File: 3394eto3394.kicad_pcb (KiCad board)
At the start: 2 copper layers, 21.5 x 31.2 mm, 11 parts, among them J1 Conn_01x20_Male, J2 Conn_01x02_Male, J3 Conn_01x02_Male, J4 Conn_01x02_Male, U1 AS3394E

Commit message: Version 2
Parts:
- removed J3, J4: Conn_01x02_Male, Connector_PinHeader_2.54mm:PinHeader_1x02_P2.54mm_Vertical
- added C1: 100n, Capacitor_THT:C_Rect_L7.0mm_W3.5mm_P2.50mm_P5.00mm, F.Cu at (57.1, 29.5)
- added C2: 100n, Capacitor_THT:C_Rect_L7.0mm_W3.5mm_P2.50mm_P5.00mm, F.Cu at (38.4, 34.4)
- J2: value Conn_01x02_Male -> Conn_01x04_Male; footprint Connector_PinHeader_2.54mm:PinHeader_1x02_P2.54mm_Vertical -> Connector_PinHeader_2.54mm:PinHeader_1x04_P2.54mm_Vertical
- R3: value 1k -> 500R
- moved J2 13.7 mm to (38.1, 43.8)
- moved D1 9.24 mm to (57.2, 42.2)
- moved D2 9.24 mm to (57.2, 37.2)
- moved D3 9.24 mm to (57.2, 47.2)
- moved D4 9.24 mm to (57.2, 52.2)
- moved R1 9.12 mm to (38.9, 37.5), turned to 180 degrees
- moved R3 7.90 mm to (52.7, 57.8), turned to 0 degrees
- moved J1 6.35 mm to (45.9, 29.8)
- moved U1 6.35 mm to (42.0, 29.8)
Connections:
- J1 pad 9: /EXT_IN -> /NOISE_IN
- J2 pad 2: GND -> /SAW_OUT
- U1 pad 11: /EXT_IN1 -> /NOISE_IN
- U1 pad 14: /EXT_IN -> /EXT_IN1
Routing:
- net /EXT_IN1: track 10.8 -> 33.9 mm, vias 0 -> 2
- net /NOISE_IN: track 0.00 -> 7.96 mm
- net /EXT_IN: track 6.61 -> 0.00 mm
- net /Cs: track 9.33 -> 15.3 mm
- net -VSW: track 3.92 -> 9.50 mm
- net +VSW: track 3.92 -> 9.18 mm
- net /SUB_OUT: track 9.53 -> 5.50 mm
- net GND: track 0.00 -> 2.74 mm
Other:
- board size 21.5 x 31.2 mm -> 25.3 x 33.4 mm

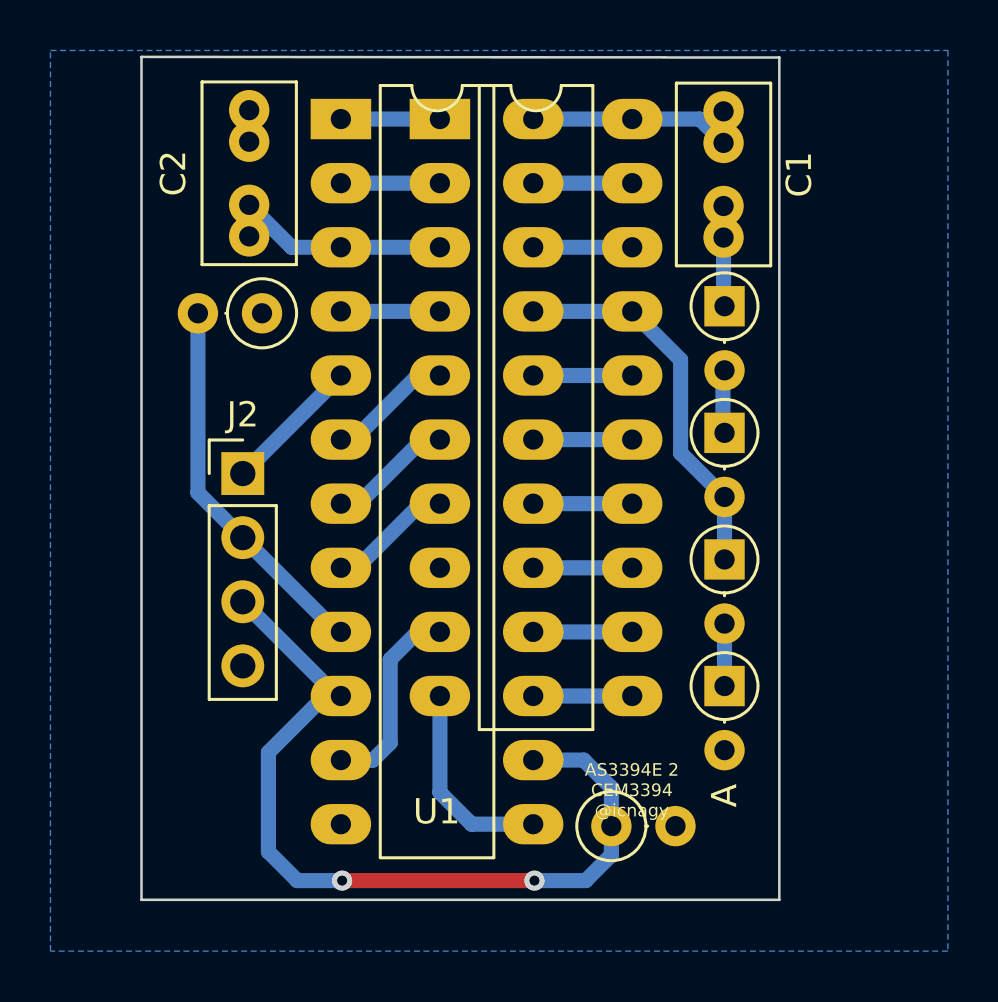
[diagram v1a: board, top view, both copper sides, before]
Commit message: Upgrade to kicad 6, add missing capacitor
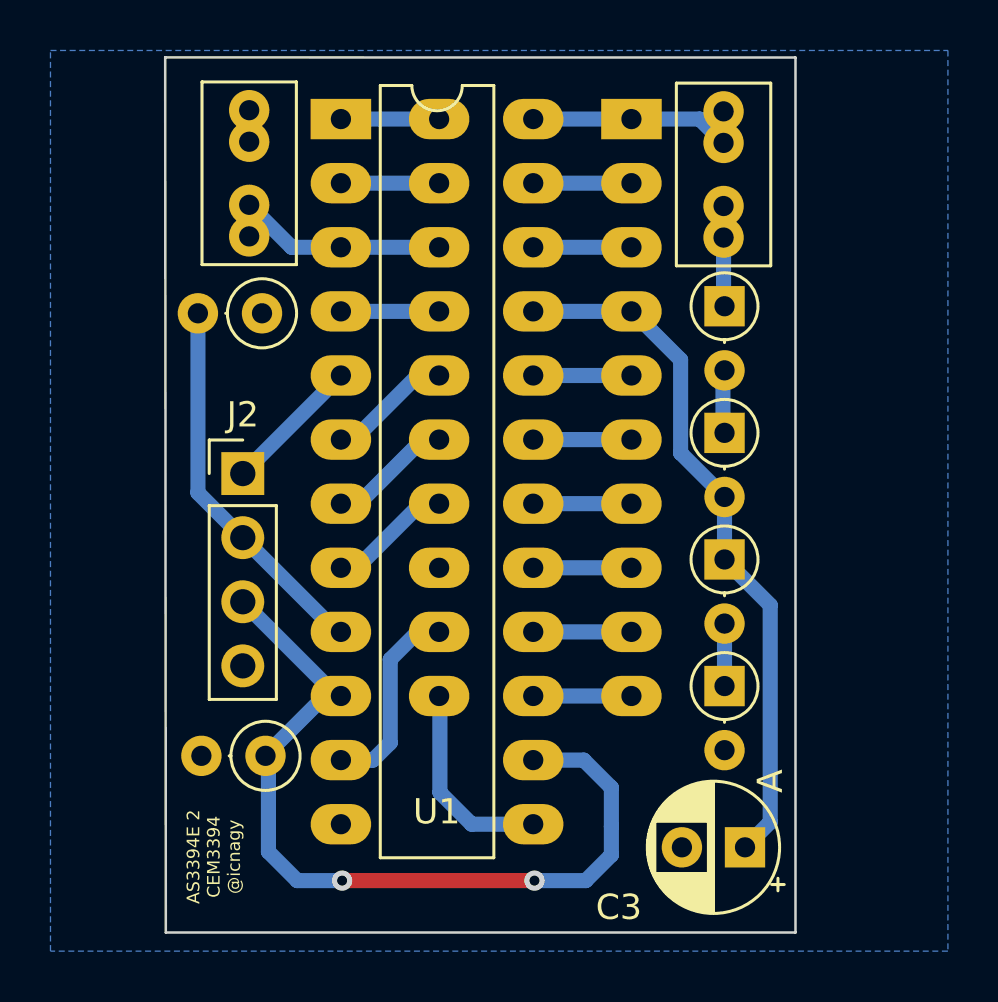
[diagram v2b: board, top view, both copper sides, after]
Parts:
- added C3: 4.7uF, Capacitor_THT:CP_Radial_D5.0mm_P2.50mm, F.Cu at (58.0, 58.6)
- J1: moved to B.Cu
- moved R3 14.0 mm to (39.0, 55.0), turned to 180 degrees
- moved J1 7.59 mm to (53.5, 29.8), turned to 180 degrees
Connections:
- C1 pad 1: +VSW -> /V+
- C2 pad 1: -VSW -> /V-
- J1 pad 1: /Iref -> /V+
- J1 pad 10: /MIX_BAL -> /VCF_Q_CV
- J1 pad 11: /VCF_Q_CV -> /MIX_BAL
- J1 pad 12: /C1 -> /NOISE_IN
- J1 pad 13: /C2 -> GND
- J1 pad 14: /C3 -> /PW
- J1 pad 15: /C4 -> /WAVE_SEL
- J1 pad 16: /VCF_CV -> /MOD_AMT
- J1 pad 17: /Cs -> /Ct
- J1 pad 18: /VCA_CV -> /V-
- J1 pad 19: /VOICE_OUT -> /VCO_CV
- J1 pad 2: /VCO_CV -> /VOICE_OUT
- J1 pad 20: +VSW -> /Iref
- J1 pad 3: -VSW -> /VCA_CV
- J1 pad 4: /Ct -> /Cs
- J1 pad 5: /MOD_AMT -> /VCF_CV
- J1 pad 6: /WAVE_SEL -> /C4
- J1 pad 7: /PW -> /C3
- J1 pad 8: GND -> /C2
- J1 pad 9: /NOISE_IN -> /C1
- U1 pad 24: +VSW -> /V+
- U1 pad 3: -VSW -> /V-
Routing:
- net /Cs: track 15.3 -> 27.8 mm
- net /V-: track 0.00 -> 9.50 mm
- net -VSW: track 9.50 -> 0.00 mm
- net /V+: track 0.00 -> 9.18 mm
- net +VSW: track 9.18 -> 0.00 mm
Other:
- board size 25.3 x 33.4 mm -> 25 x 34.7 mm
- net class Default removed
